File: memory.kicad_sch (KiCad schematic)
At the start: 0 parts

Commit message: Fixed schematic symbol errors
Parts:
- added IC601: MT40A1G16TB-062E_IT_F, symbol SoftServicesSymbolLibrary:MT40A1G16TB-062E_IT_F
- added R601: 0R, symbol Device:R
- added U601: AM6231ASGGGAALW, symbol SoftServicesSymbolLibrary:AM6231ASGGGAALW
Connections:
- new net: IC601.F9 (ZQ), R601.1
- new net DDR_A0: IC601.P3 (A0)
- new net DDR_A1: IC601.P7 (A1)
- new net DDR_A10: IC601.M3 (A10/AP)
- new net DDR_A11: IC601.T2 (A11)
- new net DDR_A12: IC601.M7 (A12/BC_N)
- new net DDR_A13: IC601.T8 (A13)
- new net DDR_A14_WEn: IC601.L2 (WE_N/A14)
- new net DDR_A15_CAS: IC601.M8 (CAS_N/A15)
- new net DDR_A16_RAS: IC601.L8 (RAS_N/A16)
- new net DDR_A2: IC601.R3 (A2)
- new net DDR_A3: IC601.N7 (A3)
- new net DDR_A4: IC601.N3 (A4)
- new net DDR_A5: IC601.P8 (A5)
- new net DDR_A6: IC601.P2 (A6)
- new net DDR_A7: IC601.R8 (A7)
- new net DDR_A8: IC601.R2 (A8)
- new net DDR_A9: IC601.R7 (A9)
- new net DDR_ACTn: IC601.L3 (ACT_N)
- new net DDR_ALERTn: IC601.P9 (ALERT_N)
- new net DDR_BA0: IC601.N2 (BA0)
- new net DDR_BA1: IC601.N8 (BA1)
- new net DDR_BG0: IC601.M2 (BG0)
- new net DDR_CKE: IC601.K2 (CKE)
- new net DDR_CLKN: IC601.K8 (CK_C)
- new net DDR_CLKP: IC601.K7 (CK_T)
- new net DDR_CSn: IC601.L7 (CS_N)
- new net DDR_DQ0: IC601.G2 (DQ0)
- new net DDR_DQ1: IC601.F7 (DQ1)
- new net DDR_DQ10: IC601.C3 (DQ10)
- new net DDR_DQ11: IC601.C7 (DQ11)
- new net DDR_DQ12: IC601.C2 (DQ12)
- new net DDR_DQ13: IC601.C8 (DQ13)
- new net DDR_DQ14: IC601.D3 (DQ14)
- new net DDR_DQ15: IC601.D7 (DQ15)
- new net DDR_DQ2: IC601.H3 (DQ2)
- new net DDR_DQ3: IC601.H7 (DQ3)
- new net DDR_DQ4: IC601.H2 (DQ4)
- new net DDR_DQ5: IC601.H8 (DQ5)
- new net DDR_DQ6: IC601.J3 (DQ6)
- new net DDR_DQ7: IC601.J7 (DQ7)
- new net DDR_DQ8: IC601.A3 (DQ8)
- new net DDR_DQ9: IC601.B8 (DQ9)
- new net DDR_LDQS_N: IC601.F3 (LDQS_C)
- new net DDR_LDQS_P: IC601.G3 (LDQS_T)
- new net DDR_ODT: IC601.K3 (ODT)
- new net DDR_PARITY: IC601.T3 (PAR)
- new net DDR_RESET#: IC601.P1 (RESET_N)
- new net DDR_TEN: IC601.N9 (TEN)
- new net DDR_UDM: IC601.E2 (NF/UDM_N/UDBI_N)
- new net DDR_UDQS_N: IC601.A7 (UDQS_C)
- new net DDR_UDQS_P: IC601.B7 (UDQS_T)
- new net DDR_VPP: IC601.B1 (VPP), IC601.M1 (VREFCA), IC601.R9 (VPP)
- new net GND: IC601.A2 (VSSQ), IC601.A8 (VSSQ), IC601.B2 (VSS), IC601.C9 (VSSQ), IC601.D2 (VSSQ), IC601.D8 (VSSQ), IC601.E1 (VSS), IC601.E3 (VSSQ), IC601.E8 (VSSQ), IC601.E9 (VSS), IC601.F1 (VSSQ), IC601.G8 (VSS), IC601.H1 (VSSQ), IC601.H9 (VSSQ), IC601.K1 (VSS), IC601.K9 (VSS), IC601.M9 (VSS), IC601.N1 (VSS), IC601.T1 (VSS), R601.2
- new net VDD_1V2: IC601.A1 (VDDQ), IC601.A9 (VDDQ), IC601.B3 (VDD), IC601.B9 (VDD), IC601.C1 (VDDQ), IC601.D1 (VDD), IC601.D9 (VDDQ), IC601.F2 (VDDQ), IC601.F8 (VDDQ), IC601.G1 (VDDQ), IC601.G7 (VDD), IC601.G9 (VDDQ), IC601.J1 (VDD), IC601.J2 (VDDQ), IC601.J8 (VDDQ), IC601.J9 (VDD), IC601.L1 (VDD), IC601.L9 (VDD), IC601.R1 (VDD), IC601.T9 (VDD)

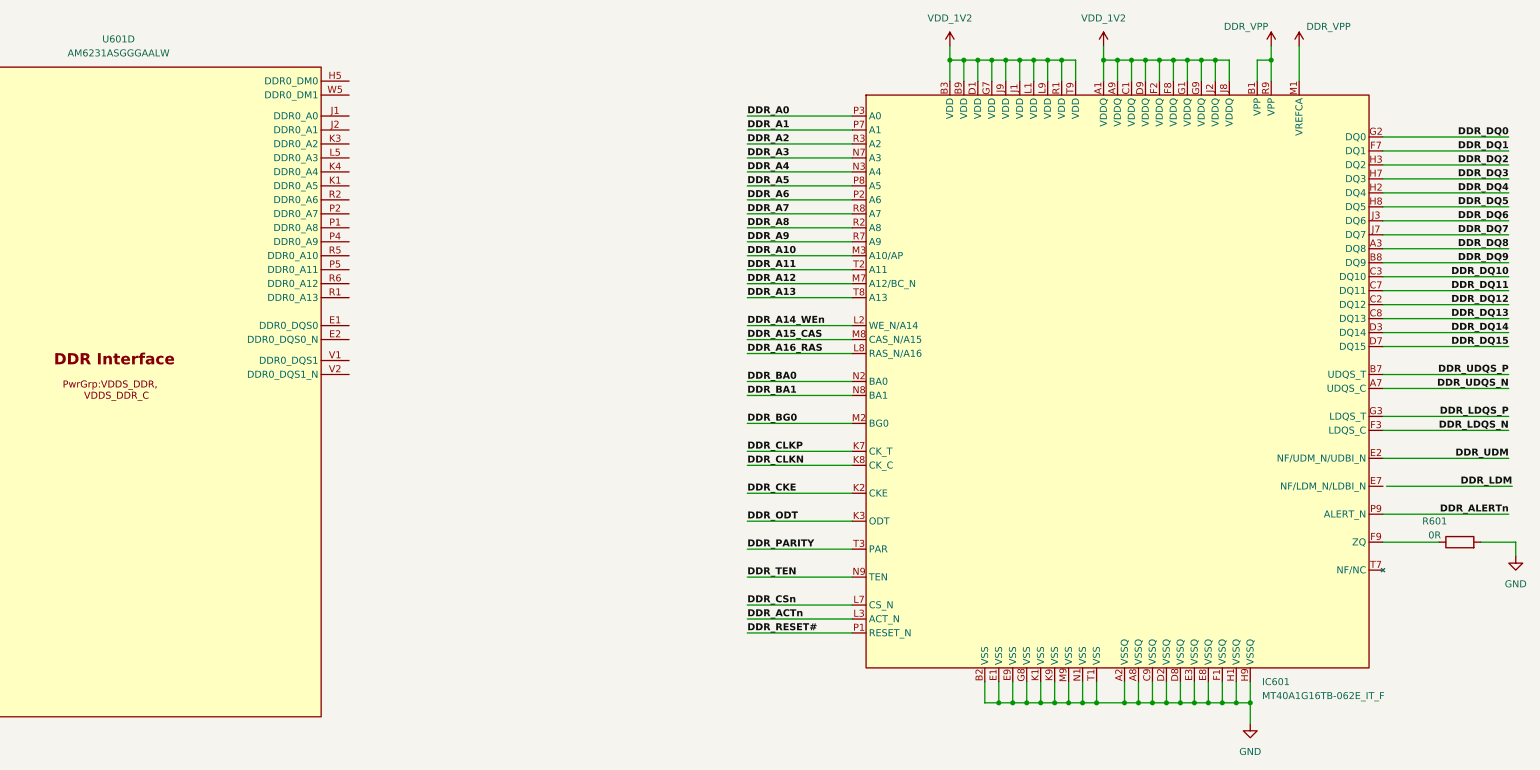
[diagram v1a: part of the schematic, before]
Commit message: Added some net labels and schematic routing
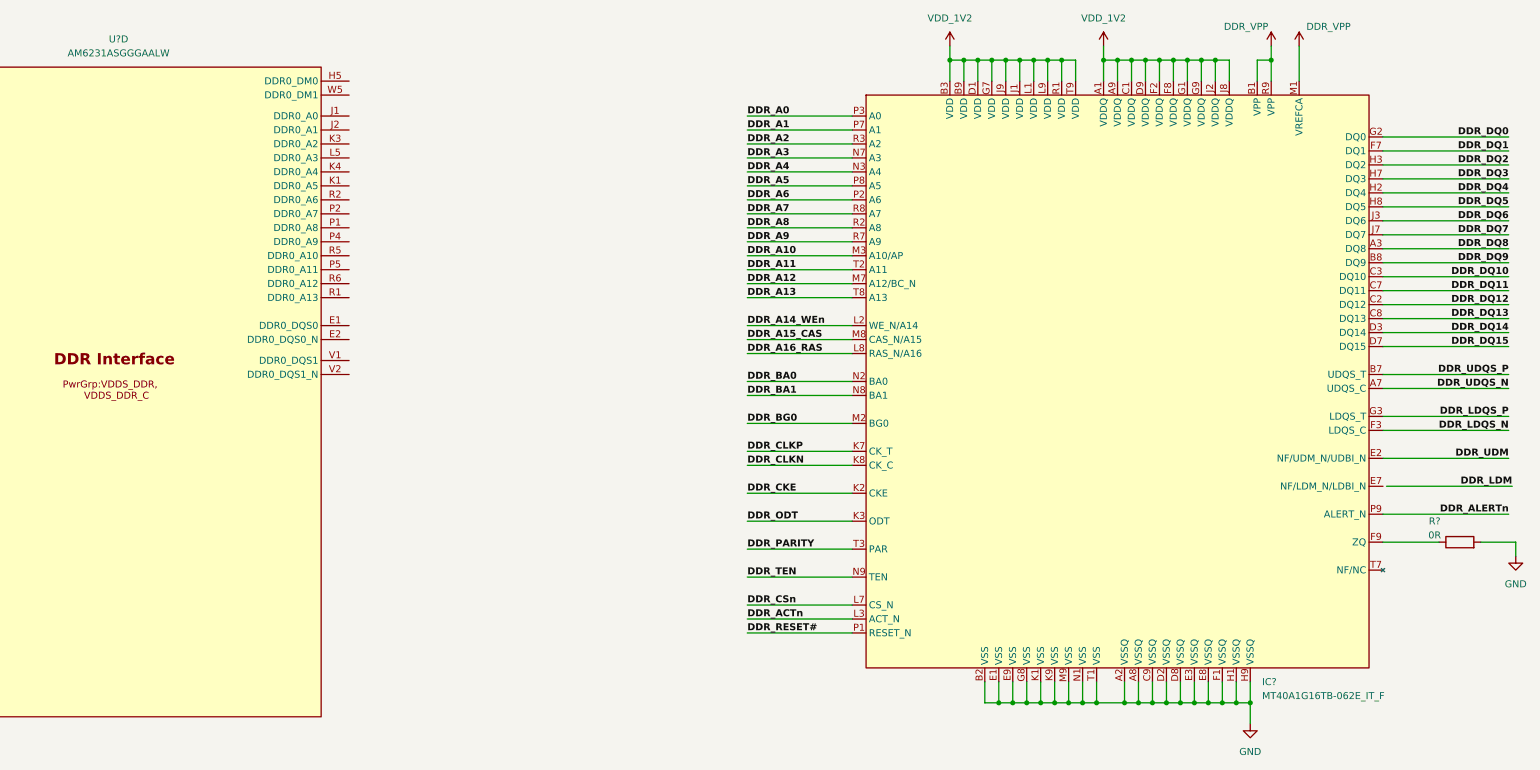
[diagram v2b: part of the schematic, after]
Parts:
- renumbered IC601 to IC?, R601 to R?, U601 to U?
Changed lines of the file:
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@@
 		(dnp no)
 		(fields_autoplaced yes)
-		(property "Reference" "IC601"
+		(property "Reference" "IC?"
 			(at 347.5833 203.2 0)
 			(effects
@@
 			(project ""
 				(path "/b43b7bca-e50d-42ec-8ff0-e0016dfefe0a/0f49ee45-e999-4887-835b-49de9bc4f6ff"
-					(reference "IC601")
+					(reference "IC?")
 					(unit 1)
 				)
@@
 		(dnp no)
 		(fields_autoplaced yes)
-		(property "Reference" "U601"
+		(property "Reference" "U?"
 			(at 139.7 86.36 0)
 			(effects
@@
 			(project "Leonhart"
 				(path "/b43b7bca-e50d-42ec-8ff0-e0016dfefe0a/0f49ee45-e999-4887-835b-49de9bc4f6ff"
-					(reference "U601")
+					(reference "U?")
 					(unit 4)
 				)
@@
 		(dnp no)
 		(fields_autoplaced yes)
-		(property "Reference" "#PWR0602"
+		(property "Reference" "#PWR0170"
 			(at 318.77 91.44 0)
 			(effects
@@
 			(project "Leonhart"
 				(path "/b43b7bca-e50d-42ec-8ff0-e0016dfefe0a/0f49ee45-e999-4887-835b-49de9bc4f6ff"
-					(reference "#PWR0602")
+					(reference "#PWR0170")
 					(unit 1)
 				)
@@
 		(on_board yes)
 		(dnp no)
-		(property "Reference" "R601"
+		(property "Reference" "R?"
 			(at 378.968 173.99 90)
 			(effects
@@
 			(project ""
 				(path "/b43b7bca-e50d-42ec-8ff0-e0016dfefe0a/0f49ee45-e999-4887-835b-49de9bc4f6ff"
-					(reference "R601")
+					(reference "R?")
 					(unit 1)
 				)
@@
 		(dnp no)
 		(fields_autoplaced yes)
-		(property "Reference" "#PWR0601"
+		(property "Reference" "#PWR0167"
 			(at 290.83 91.44 0)
 			(effects
@@
 			(project "Leonhart"
 				(path "/b43b7bca-e50d-42ec-8ff0-e0016dfefe0a/0f49ee45-e999-4887-835b-49de9bc4f6ff"
-					(reference "#PWR0601")
+					(reference "#PWR0167")
 					(unit 1)
 				)
@@
 		(dnp no)
 		(fields_autoplaced yes)
-		(property "Reference" "#PWR0603"
+		(property "Reference" "#PWR0166"
 			(at 345.44 217.17 0)
 			(effects
@@
 			(project ""
 				(path "/b43b7bca-e50d-42ec-8ff0-e0016dfefe0a/0f49ee45-e999-4887-835b-49de9bc4f6ff"
-					(reference "#PWR0603")
+					(reference "#PWR0166")
 					(unit 1)
 				)
@@
 		(on_board yes)
 		(dnp no)
-		(property "Reference" "#PWR0605"
+		(property "Reference" "#PWR0169"
 			(at 354.33 91.44 0)
 			(effects
@@
 			(project "Leonhart"
 				(path "/b43b7bca-e50d-42ec-8ff0-e0016dfefe0a/0f49ee45-e999-4887-835b-49de9bc4f6ff"
-					(reference "#PWR0605")
+					(reference "#PWR0169")
 					(unit 1)
 				)
@@
 		(on_board yes)
 		(dnp no)
-		(property "Reference" "#PWR0604"
+		(property "Reference" "#PWR0168"
 			(at 349.25 91.44 0)
 			(effects
@@
 			(project ""
 				(path "/b43b7bca-e50d-42ec-8ff0-e0016dfefe0a/0f49ee45-e999-4887-835b-49de9bc4f6ff"
-					(reference "#PWR0604")
+					(reference "#PWR0168")
 					(unit 1)
 				)
@@
 		(dnp no)
 		(fields_autoplaced yes)
-		(property "Reference" "#PWR0606"
+		(property "Reference" "#PWR0165"
 			(at 393.7 186.69 0)
 			(effects
@@
 			(project ""
 				(path "/b43b7bca-e50d-42ec-8ff0-e0016dfefe0a/0f49ee45-e999-4887-835b-49de9bc4f6ff"
-					(reference "#PWR0606")
+					(reference "#PWR0165")
 					(unit 1)
 				)

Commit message: Worked on schematic for DDR4 memory
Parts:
- added R502: R, symbol Device:R
- gave numbers to parts that had none: 3
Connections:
- net DDR_A0: no longer IC501.P3 (A0)
- net DDR_A1: no longer IC501.P7 (A1)
- net DDR_A10: no longer IC501.M3 (A10/AP)
- net DDR_A11: no longer IC501.T2 (A11)
- net DDR_A12: no longer IC501.M7 (A12/BC_N)
- net DDR_A13: no longer IC501.T8 (A13)
- net DDR_A14_WEn: now also U501.N3 (DDR0_WE_N)
- net DDR_A15_CAS: now also U501.M4 (DDR0_CAS_N)
- net DDR_A16_RAS: now also U501.M5 (DDR0_RAS_N)
- net DDR_A2: no longer IC501.R3 (A2)
- net DDR_A3: no longer IC501.N7 (A3)
- net DDR_A4: no longer IC501.N3 (A4)
- net DDR_A5: no longer IC501.P8 (A5)
- net DDR_A6: no longer IC501.P2 (A6)
- net DDR_A7: no longer IC501.R8 (A7)
- net DDR_A8: no longer IC501.R2 (A8)
- net DDR_A9: no longer IC501.R7 (A9)
- net DDR_ACTn: now also U501.N6 (DDR0_ACT_N)
- net DDR_ALERTn: now also U501.R3 (DDR0_ALERT_N)
- net DDR_BA0: now also U501.M1 (DDR0_BA0)
- net DDR_BA1: now also U501.N1 (DDR0_BA1)
- net DDR_BG0: now also U501.T4 (DDR0_BG0)
- net DDR_CKE: now also U501.H2 (DDR0_CKE0)
- net DDR_CLKN: now also U501.L2 (DDR0_CK0_N)
- net DDR_CLKP: now also U501.L1 (DDR0_CK0)
- net DDR_CSn: now also U501.L6 (DDR0_CS0_N)
- net DDR_DQ0: now also U501.F4 (DDR0_DQ0)
- net DDR_DQ1: now also U501.G5 (DDR0_DQ1)
- net DDR_DQ10: now also U501.U2 (DDR0_DQ10)
- net DDR_DQ11: now also U501.V5 (DDR0_DQ11)
- net DDR_DQ12: now also U501.W2 (DDR0_DQ12)
- net DDR_DQ13: now also U501.V6 (DDR0_DQ13)
- net DDR_DQ14: now also U501.Y1 (DDR0_DQ14)
- net DDR_DQ15: now also U501.W1 (DDR0_DQ15)
- net DDR_DQ2: now also U501.F3 (DDR0_DQ2)
- net DDR_DQ3: now also U501.H6 (DDR0_DQ3)
- net DDR_DQ4: now also U501.E3 (DDR0_DQ4)
- net DDR_DQ5: now also U501.G2 (DDR0_DQ5)
- net DDR_DQ6: now also U501.F2 (DDR0_DQ6)
- net DDR_DQ7: now also U501.F1 (DDR0_DQ7)
- net DDR_DQ8: now also U501.U1 (DDR0_DQ8)
- net DDR_DQ9: now also U501.U3 (DDR0_DQ9)
- net DDR_LDQS_N: now also U501.E2 (DDR0_DQS0_N)
- net DDR_LDQS_P: now also U501.E1 (DDR0_DQS0)
- net DDR_ODT: now also U501.H1 (DDR0_ODT0)
- net DDR_PARITY: now also U501.T1 (DDR0_PAR)
- net DDR_RESET#: now also U501.G1 (DDR0_RESET0_N)
- net DDR_UDQS_N: now also U501.V2 (DDR0_DQS1_N)
- net DDR_UDQS_P: now also U501.V1 (DDR0_DQS1)
- net GND: now also R502.1
- net at U501.J1 (DDR0_A0): now also IC501.P3 (A0)
- net at U501.J2 (DDR0_A1): now also IC501.P7 (A1)
- net at U501.K1 (DDR0_A5): now also IC501.P8 (A5)
- net at U501.K3 (DDR0_A2): now also IC501.R3 (A2)
- net at U501.K4 (DDR0_A4): now also IC501.N3 (A4)
- net at U501.L5 (DDR0_A3): now also IC501.N7 (A3)
- net at U501.M2 (DDR0_CAL0): now also R502.2
- net at U501.P1 (DDR0_A8): now also IC501.R2 (A8)
- net at U501.P2 (DDR0_A7): now also IC501.R8 (A7)
- net at U501.P4 (DDR0_A9): now also IC501.R7 (A9)
- net at U501.P5 (DDR0_A11): now also IC501.T2 (A11)
- net at U501.R1 (DDR0_A13): now also IC501.T8 (A13)
- net at U501.R2 (DDR0_A6): now also IC501.P2 (A6)
- net at U501.R5 (DDR0_A10): now also IC501.M3 (A10/AP)
- net at U501.R6 (DDR0_A12): now also IC501.M7 (A12/BC_N)
- no-connect marks 0 -> 6
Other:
- moved on the sheet: U501D

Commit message: Finished DDR4 schematic + relevant circuity and started SoC power
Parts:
- added C501: 2.2u, symbol Device:C
- added C502, C503, C517, C518, C519: 0.1u, symbol Device:C
- added C504: 22u, symbol Device:C
- added C505, C506, C507, C508, C509, C510, C511, C512, C513, C514, C515, C516, C520, C521: 0.01u, symbol Device:C
- added FB501: 120R, symbol Device:FerriteBead
- added R503, R504, R508: 1k, symbol Device:R
- added R505, R506: 39.2R, symbol Device:R
- added R507: 10k, symbol Device:R
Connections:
- net DDR_A0: now also IC501.P3 (A0), U501.J1 (DDR0_A0)
- net DDR_A1: now also IC501.P7 (A1), U501.J2 (DDR0_A1)
- net DDR_A10: now also IC501.M3 (A10/AP), U501.R5 (DDR0_A10)
- net DDR_A11: now also IC501.T2 (A11), U501.P5 (DDR0_A11)
- net DDR_A12: now also IC501.M7 (A12/BC_N), U501.R6 (DDR0_A12)
- net DDR_A13: now also IC501.T8 (A13), U501.R1 (DDR0_A13)
- net DDR_A2: now also IC501.R3 (A2), U501.K3 (DDR0_A2)
- net DDR_A3: now also IC501.N7 (A3), U501.L5 (DDR0_A3)
- net DDR_A4: now also IC501.N3 (A4), U501.K4 (DDR0_A4)
- net DDR_A5: now also IC501.P8 (A5), U501.K1 (DDR0_A5)
- net DDR_A6: now also IC501.P2 (A6), U501.R2 (DDR0_A6)
- net DDR_A7: now also IC501.R8 (A7), U501.P2 (DDR0_A7)
- net DDR_A8: now also IC501.R2 (A8), U501.P1 (DDR0_A8)
- net DDR_A9: now also IC501.R7 (A9), U501.P4 (DDR0_A9)
- net DDR_ALERTn: now also R507.1
- net DDR_CLKN: now also R506.2
- net DDR_CLKP: now also R505.2
- net DDR_TEN: now also R508.1
- net DDR_VPP: now also C501.1, C502.1, C503.1, FB501.2; no longer IC501.M1 (VREFCA)
- net GND: now also C501.2, C502.2, C503.2, C504.2, C505.2, C506.2, C507.2, C508.2, C509.2, C510.2, C511.2, C512.2, C513.2, C514.2, C515.2, C516.2, C517.2, C518.2, C520.2, R503.2, R508.2
- net VDD_1V2: now also C504.1, C505.1, C506.1, C507.1, C508.1, C509.1, C510.1, C511.1, C512.1, C513.1, C514.1, C515.1, C516.1, C519.2, C521.1, R504.2
- new net: C521.2, R505.1, R506.1
- new net DDR_VREFCA: C517.1, C518.1, C519.1, C520.1, IC501.M1 (VREFCA), R503.1, R504.1
- new net VDD_2V5: FB501.1
- new net VDD_DDR4: R507.2
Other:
- moved on the sheet: IC501, R501, R502, U501D

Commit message: Added thread circuitry
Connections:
- net GND: no longer C505.2
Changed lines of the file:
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@@
 	(generator_version "9.0")
 	(paper "A2")
-	(text_box "SOC DDR4 Interface and DDR4 Device"
+	(text_box "Decoupling Capacitors + Revelant Circuitry"
 		(exclude_from_sim no)
-		(at 30.48 80.01 0)
-		(size 361.95 204.47)
+		(at 402.59 80.01 0)
+		(size 147.955 204.47)
 		(margins 0.9525 0.9525 0.9525 0.9525)
 		(stroke
@@
 		)
 	)
-	(text_box "Decoupling Capacitors + Revelant Circuitry"
-		(exclude_from_sim no)
-		(at 402.59 80.01 0)
-		(size 147.955 204.47)
-		(margins 0.9525 0.9525 0.9525 0.9525)
-		(stroke
-			(width 0)
-			(type solid)
-		)
-		(fill
-			(type none)
-		)
-		(effects
-			(font
-				(size 5.08 5.08)
-				(thickness 1.016)
-				(bold yes)
-			)
-			(justify left top)
-		)
-	)
 	(junction
 		(at 298.45 119.38)
@@
 	(junction
 		(at 299.72 236.22)
-		(diameter 0)
-		(color 0 0 0 0)
-	)
-	(junction
-		(at 429.26 151.13)
 		(diameter 0)
 		(color 0 0 0 0)
@@
 	(wire
 		(pts
-			(xy 429.26 148.59) (xy 429.26 151.13)
-		)
-		(stroke
-			(width 0)
-			(type default)
-		)
-	)
-	(wire
-		(pts
 			(xy 416.56 106.68) (xy 416.56 109.22)
 		)
@@
 	(wire
 		(pts
-			(xy 429.26 151.13) (xy 441.96 151.13)
-		)
-		(stroke
-			(width 0)
-			(type default)
-		)
-	)
-	(wire
-		(pts
 			(xy 284.48 232.41) (xy 284.48 236.22)
 		)
@@
 	(wire
 		(pts
-			(xy 416.56 151.13) (xy 429.26 151.13)
-		)
-		(stroke
+			(xy 416.56 151.13) (xy 441.96 151.13)
+		)
+		(stroke

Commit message: Tidied up schematic
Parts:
- added R509: R, symbol Device:R
- added R510: 2.2k, symbol Device:R
- R502: value R -> 240R
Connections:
- net DDR_LDM: now also U501.H5 (DDR0_DM0)
- net DDR_RESET#: now also R509.2, R510.1
- net DDR_UDM: now also U501.W5 (DDR0_DM1)
- net GND: now also R510.2
- net VDD_1V2: now also R509.1
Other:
- note added: "Decoupling Capacitors + Revelant Circuitry"
- note added: "SoC DDR Interface + DDR4 Device"
- moved on the sheet: IC501, R501, R502, U501D

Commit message: Fixed SoC power circuitry
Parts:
- added C5022, C5023: 1n, symbol Device:C
- added C5024, C5025: 100p, symbol Device:C
- added C5026, C5027: 47p, symbol Device:C
- added C5028, C5029, C5030: 10p, symbol Device:C
- C5006: renamed from C505; value 0.01u -> 0.1u
- C5007: renamed from C506; value 0.01u -> 0.1u
- C5008: renamed from C507; value 0.01u -> 0.1u
- C5009: renamed from C508; value 0.01u -> 0.1u
- C5010: renamed from C509; value 0.01u -> 0.1u
- C5011: renamed from C510; value 0.01u -> 0.1u
- C5012: renamed from C511; value 0.01u -> 0.1u
- C5013: renamed from C512; value 0.01u -> 0.1u
- C5014: renamed from C513; value 0.01u -> 0.1u
- C5015: renamed from C514; value 0.01u -> 0.1u
- C5016: renamed from C515; value 0.01u -> 0.1u
- C5017: renamed from C516; value 0.01u -> 0.1u
- R5001: renamed from R505; value 39.2R -> 33R
- R5002: renamed from R506; value 39.2R -> 33R
- renumbered C501 to C5001, C502 to C5002, C503 to C5003, C521 to C5004, C504 to C5005, C519 to C5018, C520 to C5019, C517 to C5020, C518 to C5021, FB501 to FB5001, IC501 to IC5001, R509 to R5003, R510 to R5004, R501 to R5005, R504 to R5006, R502 to R5007, R503 to R5008, R507 to R5009, R508 to R5010, U501 to U5001
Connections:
- net GND: now also C5006.2, C5022.2, C5023.2, C5024.2, C5025.2, C5026.2, C5027.2, C5028.2, C5029.2, C5030.2
- net VDD_1V2: now also C5022.1, C5023.1, C5024.1, C5025.1, C5026.1, C5027.1, C5028.1, C5029.1, C5030.1
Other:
- note added: "DDR Device"
- note added: "SoC"
- moved on the sheet: C5001, C5002, C5003, C5004, C5005, C5006, C5007, C5008, C5009, C5010, C5011, C5012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

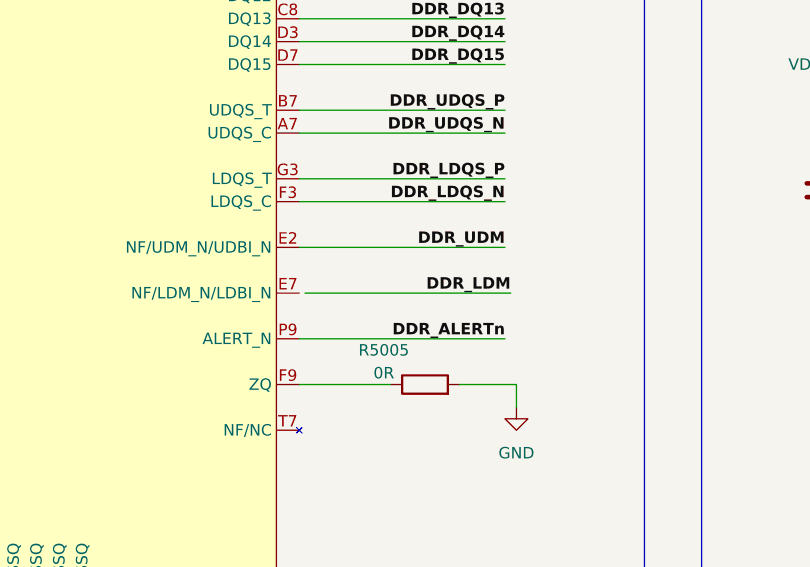
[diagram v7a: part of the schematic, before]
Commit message: Finished overall schematic. Fixing errors and warnings from ERC
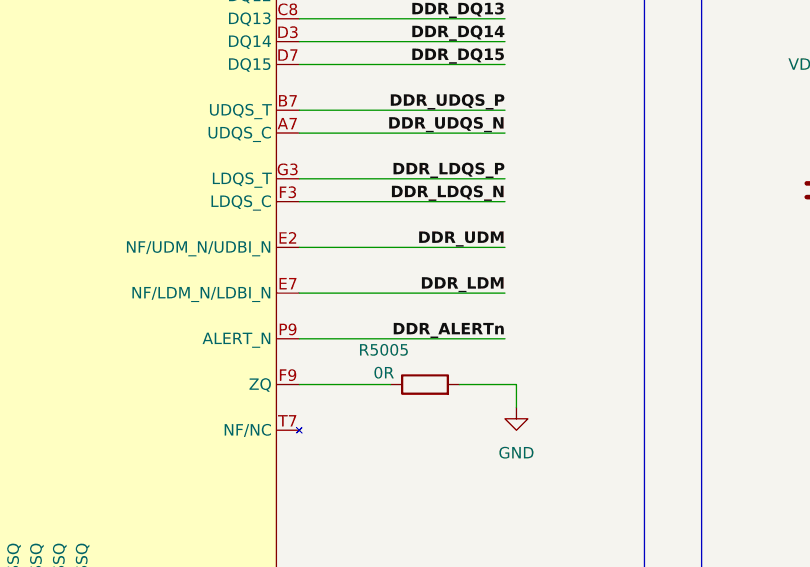
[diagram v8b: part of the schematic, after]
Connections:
- net DDR_LDM: now also IC5001.E7 (NF/LDM_N/LDBI_N)
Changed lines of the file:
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@@
+	(wire
+		(pts
+			(xy 358.14 196.85) (xy 381 196.85)
+		)
+		(stroke
+			(width 0)
+			(type default)
+		)
+	)
 	(wire
 		(pts
@@
 		(pts
 			(xy 68.58 165.1) (xy 91.44 165.1)
-		)
-		(stroke
-			(width 0)
-			(type default)
-		)
-	)
-	(wire
-		(pts
-			(xy 358.775 196.85) (xy 381.635 196.85)
 		)
 		(stroke
@@
 		)
 	)
-	(label "DDR_LDM"
-		(at 381.635 196.85 180)
-		(effects
-			(font
-				(size 1.27 1.27)
-				(thickness 0.254)
-				(bold yes)
-			)
-			(justify right bottom)
-		)
-	)
 	(label "DDR_DQ4"
 		(at 381 143.51 180)
@@
 		)
 	)
+	(label "DDR_LDM"
+		(at 381 196.85 180)
+		(effects
+			(font
+				(size 1.27 1.27)
+				(thickness 0.254)
+				(bold yes)
+			)
+			(justify right bottom)
+		)
+	)
